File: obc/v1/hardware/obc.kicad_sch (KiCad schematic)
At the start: 41 parts, among them J4 USB_C_Receptacle_USB2.0_16P, U10 LM66100DCK, U11 LM66100DCK, U12 USBLC6-2P6, U9 AMS1117-3.3

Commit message: fixes
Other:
- removed sheet FRAM Memory
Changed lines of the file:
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@@
-	)
-	(sheet
-		(at 63.5 151.13)
-		(size 13.97 10.16)
-		(exclude_from_sim no)
-		(in_bom yes)
-		(on_board yes)
-		(dnp no)
-		(fields_autoplaced yes)
-		(stroke
-			(width 0.1524)
-			(type solid)
-		)
-		(fill
-			(color 0 0 0 0)
-		)
-		(property "Sheetname" "FRAM Memory"
-			(at 63.5 150.4184 0)
-			(show_name no)
-			(do_not_autoplace no)
-			(effects
-				(font
-					(size 1.27 1.27)
-				)
-				(justify left bottom)
-			)
-		)
-		(property "Sheetfile" "fram_memory.kicad_sch"
-			(at 63.5 161.8746 0)
-			(show_name no)
-			(do_not_autoplace no)
-			(effects
-				(font
-					(size 1.27 1.27)
-				)
-				(justify left top)
-			)
-		)
-		(pin "MOSI" input
-			(at 63.5 153.67 180)
-			(effects
-				(font
-					(size 1.27 1.27)
-				)
-				(justify left)
-			)
-		)
-		(pin "SCK" input
-			(at 63.5 156.21 180)
-			(effects
-				(font
-					(size 1.27 1.27)
-				)
-				(justify left)
-			)
-		)
-		(pin "~{CS}" input
-			(at 63.5 158.75 180)
-			(effects
-				(font
-					(size 1.27 1.27)
-				)
-				(justify left)
-			)
-		)
-		(pin "MISO" output
-			(at 77.47 153.67 0)
-			(effects
-				(font
-					(size 1.27 1.27)
-				)
-				(justify right)
-			)
-		)
-		(instances
-			(project "obc"
-				(path "/ba4f88ff-24aa-49a3-8871-8c7e48b371c5"
-					(page "10")
-				)
-			)
-		)
 	)
 	(sheet

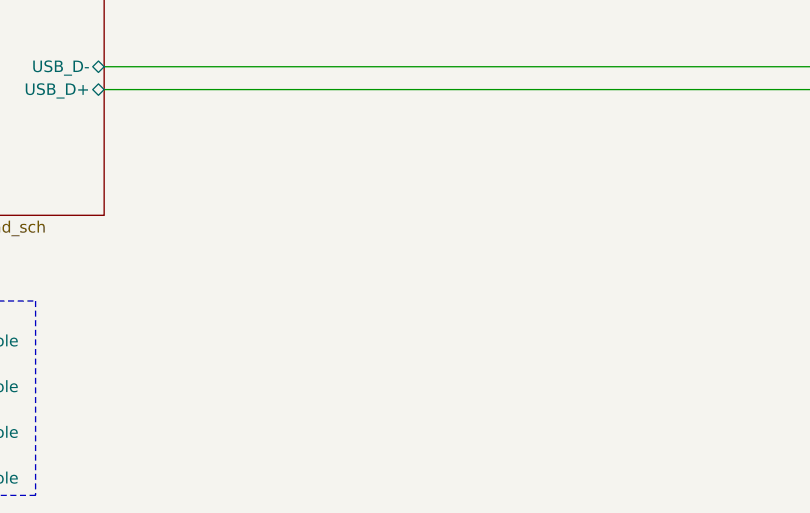
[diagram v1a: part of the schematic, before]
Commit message: FRAM Symbol & Schematic
FM25V02A:
-Created symbol & Schematic
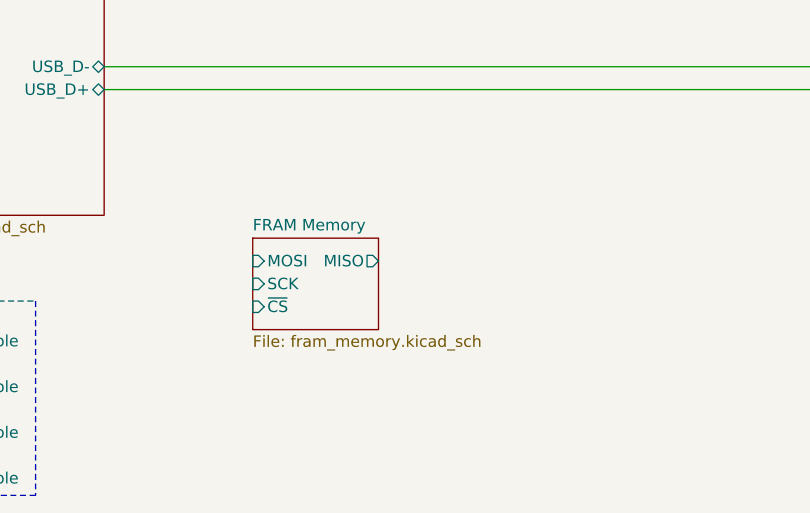
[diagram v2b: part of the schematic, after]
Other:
- added sheet FRAM Memory (fram_memory.kicad_sch)
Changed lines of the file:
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@@
+	)
+	(sheet
+		(at 63.5 151.13)
+		(size 13.97 10.16)
+		(exclude_from_sim no)
+		(in_bom yes)
+		(on_board yes)
+		(dnp no)
+		(fields_autoplaced yes)
+		(stroke
+			(width 0.1524)
+			(type solid)
+		)
+		(fill
+			(color 0 0 0 0)
+		)
+		(property "Sheetname" "FRAM Memory"
+			(at 63.5 150.4184 0)
+			(show_name no)
+			(do_not_autoplace no)
+			(effects
+				(font
+					(size 1.27 1.27)
+				)
+				(justify left bottom)
+			)
+		)
+		(property "Sheetfile" "fram_memory.kicad_sch"
+			(at 63.5 161.8746 0)
+			(show_name no)
+			(do_not_autoplace no)
+			(effects
+				(font
+					(size 1.27 1.27)
+				)
+				(justify left top)
+			)
+		)
+		(pin "MOSI" input
+			(at 63.5 153.67 180)
+			(effects
+				(font
+					(size 1.27 1.27)
+				)
+				(justify left)
+			)
+		)
+		(pin "SCK" input
+			(at 63.5 156.21 180)
+			(effects
+				(font
+					(size 1.27 1.27)
+				)
+				(justify left)
+			)
+		)
+		(pin "~{CS}" input
+			(at 63.5 158.75 180)
+			(effects
+				(font
+					(size 1.27 1.27)
+				)
+				(justify left)
+			)
+		)
+		(pin "MISO" output
+			(at 77.47 153.67 0)
+			(effects
+				(font
+					(size 1.27 1.27)
+				)
+				(justify right)
+			)
+		)
+		(instances
+			(project "obc"
+				(path "/ba4f88ff-24aa-49a3-8871-8c7e48b371c5"
+					(page "10")
+				)
+			)
+		)
 	)
 	(sheet
